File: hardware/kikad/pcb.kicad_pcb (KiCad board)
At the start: 2 copper layers, 55 x 55 mm, 22 parts, among them J1 Output

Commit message: implement binary build
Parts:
- D1, D2, D3, D4: footprint LED_THT:LED_D5.0mm-4_RGB_Wide_Pins -> LED_THT:LED_D5.0mm-4_RGB_Wide_Pins_CNC_read
- R1, R10, R11, R12, R13, R14, R2, R3, R4, R5, R6, R7, R8, R9: footprint Resistor_THT:R_Axial_DIN0204_L3.6mm_D1.6mm_P7.62mm_Horizontal -> Resistor_THT:CNC_Ready_R_Axial_DIN0204_L3.6mm_D1.6mm_P7.62mm_Horizontal
- U2: footprint esp_32_c3_supper_mini:PN532 NFC RFID -> esp_32_c3_supper_mini:PN532 NFC RFID simple (one row)
- moved BZ1 34.0 mm to (111.1, 60.2), turned to 180 degrees
- moved R13 18.4 mm to (122.5, 51.9), turned to 180 degrees
- moved R1 6.51 mm to (128.2, 42.8)
- moved R2 4.37 mm to (128.4, 45.5)
- moved R3 2.75 mm to (128.5, 48.4)
- moved D3 1.59 mm to (144.4, 92.1)
- moved D1 1.49 mm to (145.0, 43.6)
- moved D4 1.46 mm to (110.1, 92.0)
- moved R4 1.16 mm to (120.8, 48.3)
- moved R9 1.12 mm to (128.3, 93.0)
- moved R12 1.12 mm to (121.3, 93.0)
- moved D2 0.92 mm to (110.1, 43.4)
- moved R8 0.71 mm to (128.2, 90.3)
- moved R11 0.70 mm to (121.3, 90.3)
- moved R5 0.62 mm to (120.8, 45.5)
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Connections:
- R13 pad 1: Net-(U1-GPIO9/SCL) -> Net-(U1-GPIO21)
- U1 pad 13: Net-(U1-GPIO9/SCL) -> /R
- U1 pad 14: /R -> /G
- U1 pad 15: /G -> /B
- U1 pad 16: /B -> Net-(U1-GPIO21)
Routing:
- net Net-(U1-GPIO21): track 0.00 -> 20.1 mm
- net /R: track 105.5 -> 98.0 mm
- net Net-(U1-GPIO9/SCL): track 7.43 -> 0.00 mm
- net /G: track 91.3 -> 85.8 mm
- net /B: track 80.8 -> 75.5 mm
- net Net-(U1-GPIO8/SDA): track 21.9 -> 26.5 mm
- net Net-(D1-RA): track 4.93 -> 9.50 mm
- net Net-(U1-GPIO6/MOSI): track 24.0 -> 28.5 mm
- net Net-(U1-GPIO7/SS): track 20.4 -> 24.5 mm
- net Net-(U1-GPIO5/MISO): track 27.6 -> 31.1 mm
- net Net-(BZ1-+): track 6.59 -> 9.78 mm
- net Net-(D1-GA): track 12.5 -> 15.5 mm
- net Net-(D1-BA): track 17.4 -> 19.3 mm
- net Net-(D3-RA): track 10.3 -> 8.91 mm
- net Net-(D3-GA): track 16.3 -> 15.2 mm
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
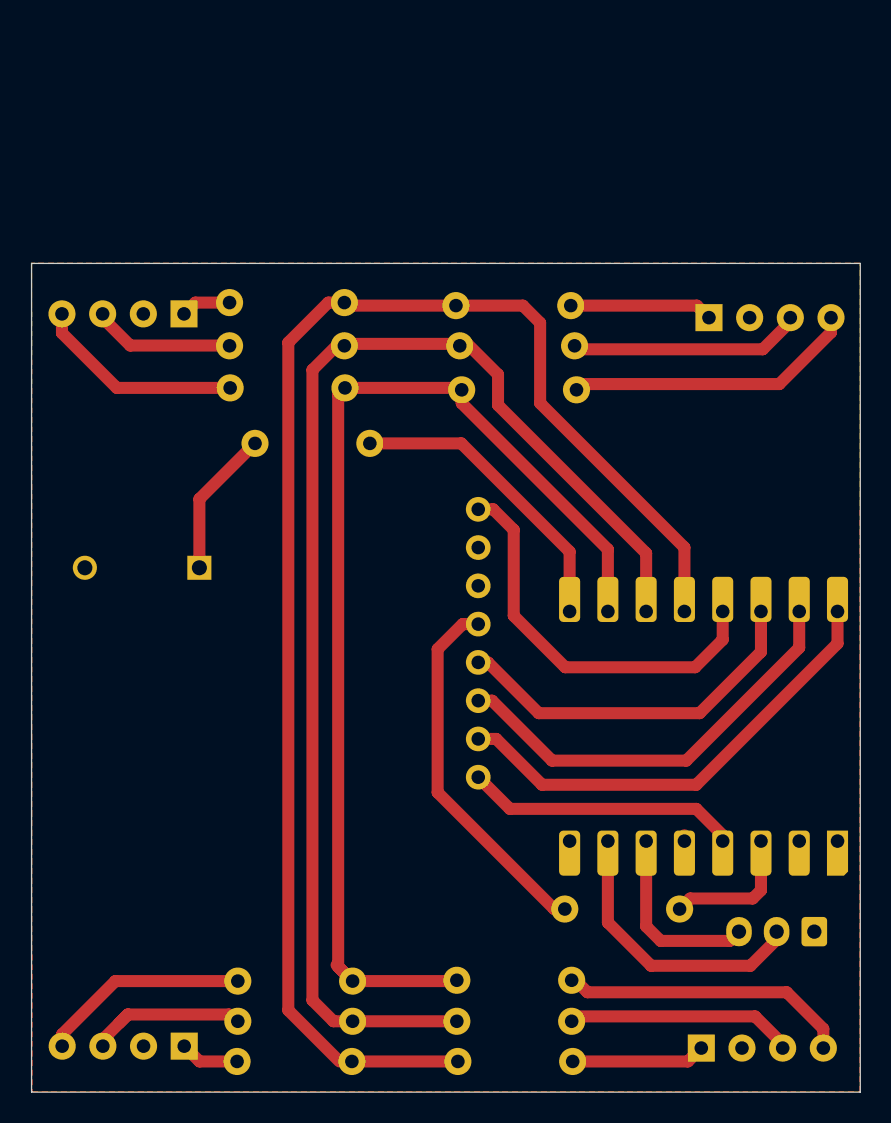
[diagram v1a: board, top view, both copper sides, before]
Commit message: update the kikad pcb, move buzzer to GPIO0
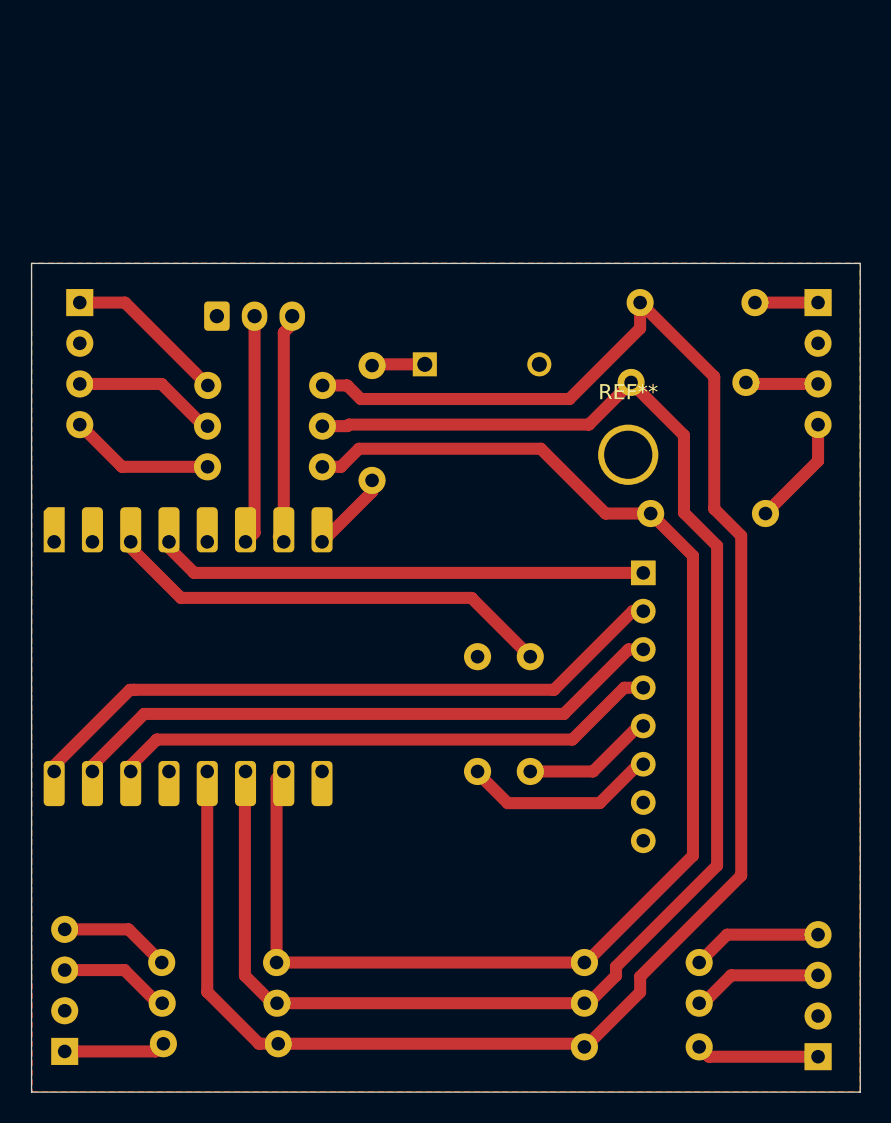
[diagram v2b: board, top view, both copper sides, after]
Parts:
- added R15: 0, Resistor_THT:CNC_Ready_R_Axial_DIN0204_L3.6mm_D1.6mm_P7.62mm_Horizontal, B.Cu at (129.6, 73.7)
- added REF**: MountingHole_3.2mm_M3, MountingHole:MountingHole_3.2mm_M3, F.Cu at (139.6, 52.7)
- moved J1 56.9 mm to (112.3, 43.5), turned to 0 degrees
- moved U1 32.3 mm to (111.5, 66.1), turned to -90 degrees
- moved BZ1 20.2 mm to (126.1, 46.7), turned to 0 degrees
- moved R3 15.0 mm to (141.1, 56.6)
- moved R1 12.2 mm to (140.4, 42.6)
- moved R2 11.6 mm to (139.8, 47.9)
- moved U2 9.91 mm to (127.1, 67.1), turned to -90 degrees
- moved R14 9.41 mm to (133.1, 73.7), turned to 90 degrees
- moved R8 8.55 mm to (136.7, 89.1)
- moved R7 8.55 mm to (136.7, 86.4)
- moved R9 8.45 mm to (136.7, 92.0)
- moved D4 7.94 mm to (102.2, 92.3), turned to 90 degrees
- moved D3 7.77 mm to (152.2, 92.7), turned to 90 degrees
- moved D1 7.31 mm to (152.2, 42.6), turned to -90 degrees
- moved D2 6.96 mm to (103.2, 42.6), turned to -90 degrees
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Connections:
- R13 pad 1: Net-(U1-GPIO21) -> Net-(U1-GPIO0)
- U1 pad 12: Net-(U1-GPIO8/SDA) -> unconnected-(U1-GPIO8/SDA-Pad12)
- U1 pad 16: Net-(U1-GPIO21) -> unconnected-(U1-GPIO21-Pad16)
- U1 pad 6: Net-(J1-Pin_3) -> Net-(J1-Pin_2)
- U1 pad 7: Net-(J1-Pin_2) -> Net-(J1-Pin_3)
- U1 pad 8: unconnected-(U1-GPIO0-Pad8) -> Net-(U1-GPIO0)
- U2 pad 10: GND -> Net-(R15-Pad1)
- U2 pad 12: Net-(U1-GPIO8/SDA) -> unconnected-(U2-RSTO-Pad12)
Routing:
- net Net-(U1-GPIO8/SDA): track 26.5 -> 0.00 mm
- net /R: track 98.0 -> 122.8 mm
- net Net-(U1-3V3): track 9.18 -> 29.9 mm
- net /G: track 85.8 -> 106.1 mm
- net Net-(U1-GPIO21): track 20.1 -> 0.00 mm
- net /B: track 75.5 -> 91.6 mm
- net Net-(R14-Pad1): track 24.9 -> 8.75 mm
- net Net-(U1-GPIO4/SCK): track 18.2 -> 32.6 mm
- net Net-(R15-Pad1): track 0.00 -> 12.9 mm
- net Net-(U1-GPIO5/MISO): track 31.1 -> 43.7 mm
- net Net-(U1-GPIO7/SS): track 24.5 -> 36.6 mm
- net Net-(D1-BA): track 19.3 -> 7.35 mm
- net Net-(U1-GPIO6/MOSI): track 28.5 -> 40.1 mm
- net Net-(D1-GA): track 15.5 -> 4.83 mm
- net Net-(D3-BA): track 19.3 -> 8.66 mm
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
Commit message: ad power for 5v esp
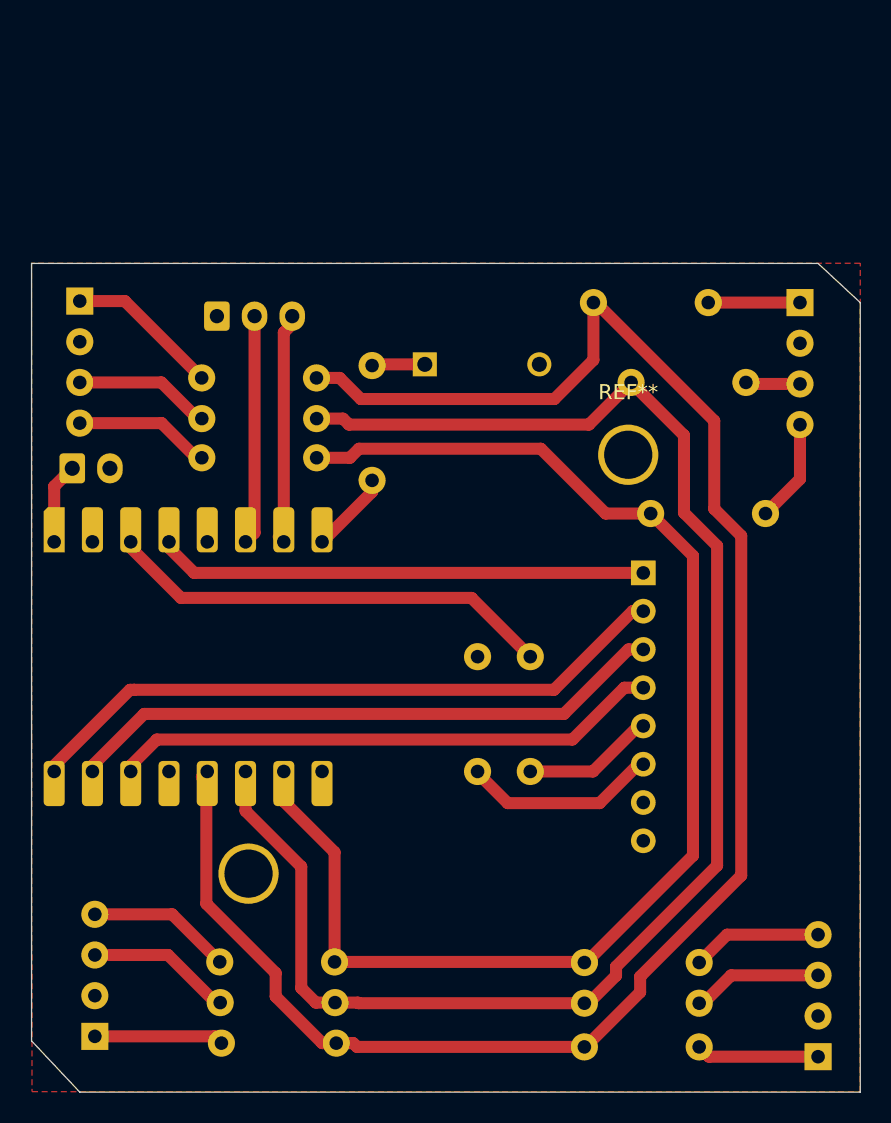
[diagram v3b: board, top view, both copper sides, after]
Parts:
- added ?: , , F.Cu at (114.4, 80.5)
- added J2: Conn_01x02_Pin, Connector_JST:JST_EH_B2B-EH-A_1x02_P2.50mm_Vertical, B.Cu at (102.7, 53.6)
- moved R10 3.85 mm to (120.1, 86.4)
- moved R11 3.85 mm to (120.1, 89.1)
- moved R12 3.85 mm to (120.2, 91.8)
- moved R1 3.10 mm to (137.3, 42.6)
- moved D4 2.24 mm to (104.2, 91.3)
- moved D1 1.20 mm to (151.0, 42.6)
- moved R4 0.71 mm to (118.9, 52.9)
- moved R6 0.65 mm to (118.9, 47.6)
- moved R5 0.63 mm to (118.9, 50.3)
- moved D2 0.10 mm to (103.2, 42.5)
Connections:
- U1 pad 1: unconnected-(U1-5V-Pad1) -> Net-(J2-Pin_1)
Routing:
- net Net-(J2-Pin_1): track 0.00 -> 5.38 mm
- net /B: track 91.6 -> 89.1 mm
- net Net-(D4-GA): track 7.38 -> 9.63 mm
- net Net-(D4-BA): track 7.35 -> 9.60 mm
- net Net-(D1-RA): track 4.19 -> 6.09 mm
- net Net-(D4-RA): track 6.76 -> 8.59 mm
- net /R: track 122.8 -> 121.3 mm
- net /G: track 106.1 -> 104.7 mm
- net Net-(D1-GA): track 4.83 -> 3.63 mm
- net Net-(D2-BA): track 9.78 -> 9.05 mm
- net Net-(D2-RA): track 10.8 -> 10.2 mm
- net Net-(D2-GA): track 9.64 -> 9.09 mm
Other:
- outline, holes or cut-outs redrawn

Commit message: use mac adress to create the prismo host and wifi
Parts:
- removed ?: , 
- removed J1: Output, Connector_JST:JST_XH_B3B-XH-A_1x03_P2.50mm_Vertical
- removed J2: Conn_01x02_Pin, Connector_JST:JST_EH_B2B-EH-A_1x02_P2.50mm_Vertical
- removed the REF** at (139.6, 52.7)
- added J3: Conn_01x04_Pin, TerminalBlock_Phoenix:TerminalBlock_Phoenix_MKDS-1,5-4-5.08_1x04_P5.08mm_Horizontal, F.Cu at (108.2, 31.9)
- added REF**: MountingHole_3.2mm_M3_DIN965, MountingHole:MountingHole_3.2mm_M3_DIN965, F.Cu at (114.4, 80.5)
- added REF**: MountingHole_3.2mm_M3_DIN965, MountingHole:MountingHole_3.2mm_M3_DIN965, F.Cu at (139.6, 52.7)
- D1, D2, D3, D4: footprint LED_THT:LED_D5.0mm-4_RGB_Wide_Pins_CNC_read -> LED_THT:LED_D5.0mm-4_RGB_Wide_Pins_CNC_read_angle
- moved D2 5.41 mm to (101.7, 47.7), turned to 90 degrees
- moved D3 5.40 mm to (146.8, 92.8)
- moved D4 4.27 mm to (108.2, 92.8), turned to 180 degrees
- moved D1 3.71 mm to (147.4, 41.7), turned to 0 degrees
- moved R9 1.52 mm to (135.3, 92.6)
- moved R12 0.88 mm to (120.2, 92.6)
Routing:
- net /R: track 121.3 -> 101.0 mm
- net Net-(J3-Pin_3): track 15.7 -> 0.42 mm
- net Net-(J3-Pin_4): track 15.7 -> 0.48 mm
- net Net-(D2-RA): track 10.2 -> 0.00 mm
- net Net-(D2-GA): track 9.09 -> 0.28 mm
- net Net-(D2-BA): track 9.05 -> 0.37 mm
- net Net-(D3-BA): track 8.66 -> 0.00 mm
- net Net-(D3-GA): track 8.66 -> 0.27 mm
- net Net-(D3-RA): track 8.16 -> 0.00 mm
- net Net-(D1-BA): track 6.85 -> 0.00 mm
- net Net-(D1-RA): track 6.09 -> 0.00 mm
- net Net-(J3-Pin_2): track 5.38 -> 0.00 mm
- net Net-(D4-RA): track 8.59 -> 4.46 mm
- net Net-(D1-GA): track 3.63 -> 0.14 mm
- net /B: track 89.1 -> 90.9 mm
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
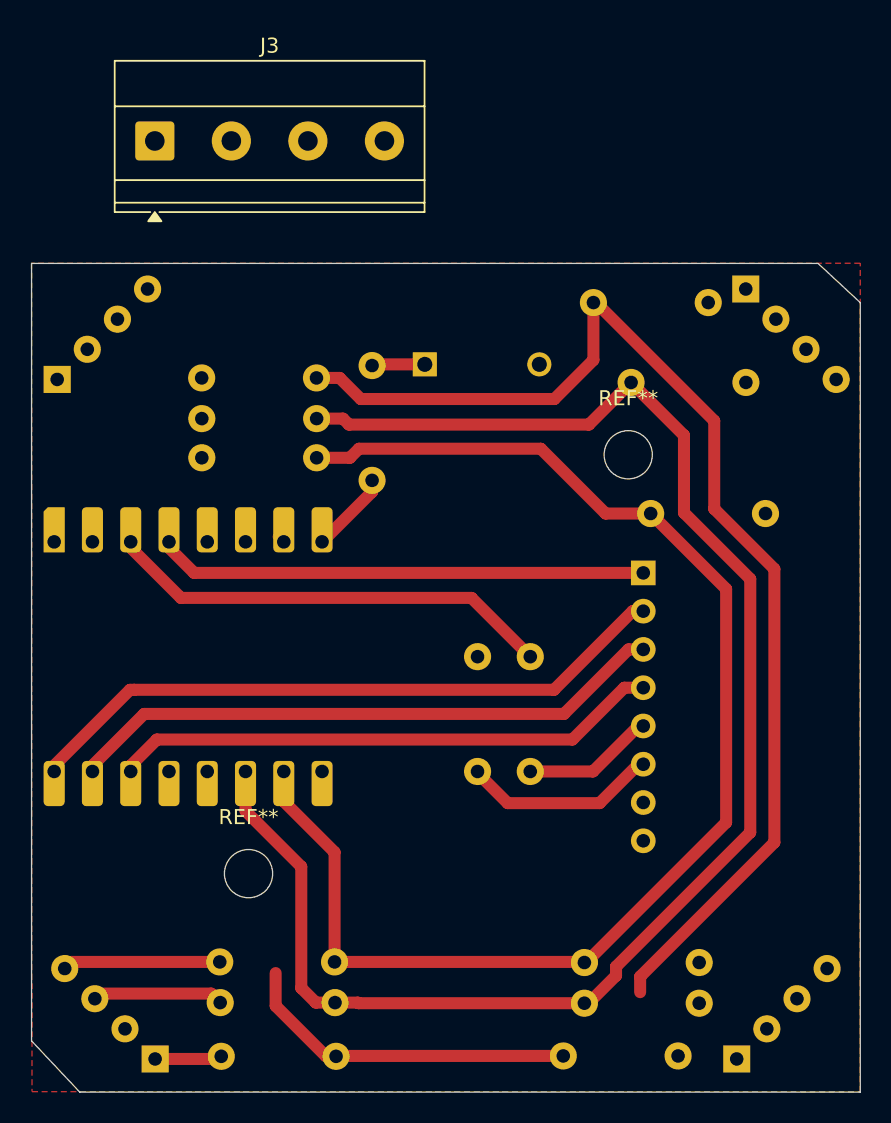
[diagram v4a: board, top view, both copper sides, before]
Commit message: new board, bottom layer, cut all corvers
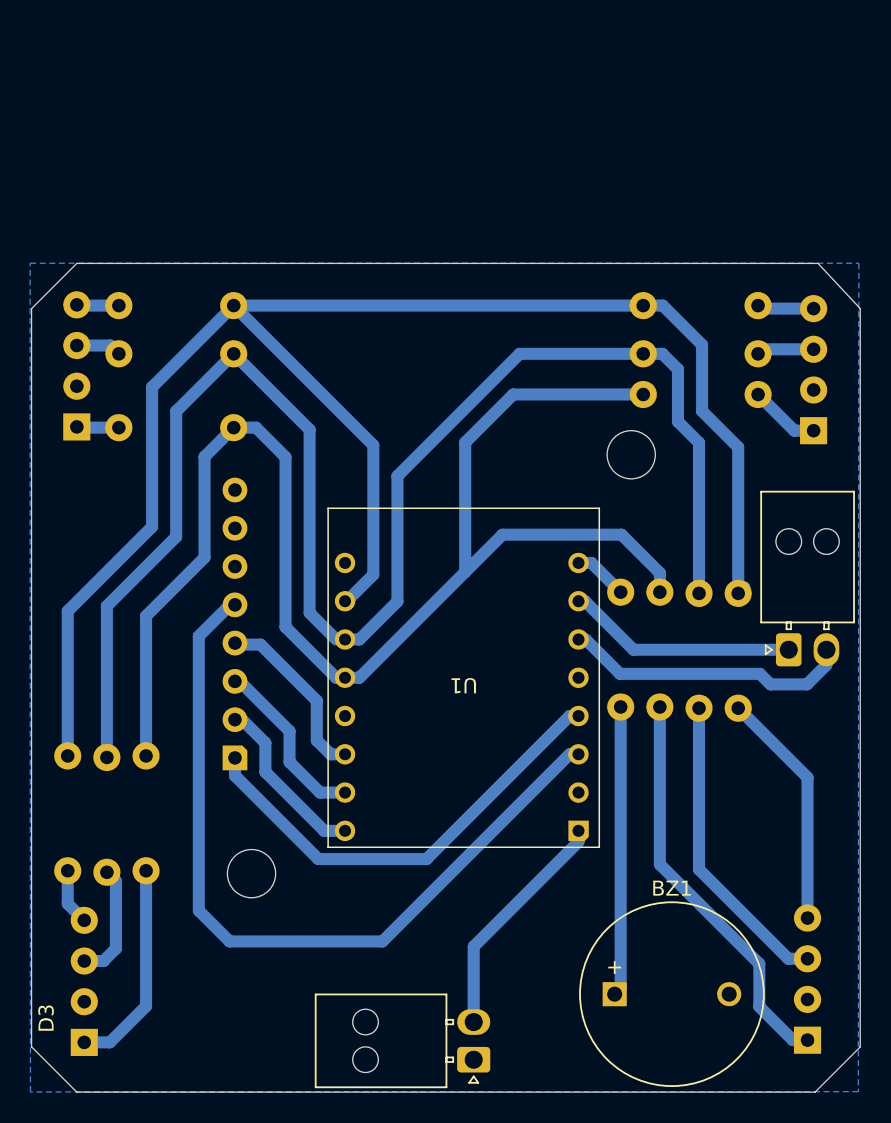
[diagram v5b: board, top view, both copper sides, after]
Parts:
- removed J3: Conn_01x04_Pin, TerminalBlock_Phoenix:TerminalBlock_Phoenix_MKDS-1,5-4-5.08_1x04_P5.08mm_Horizontal
- removed R14, R15: 0, Resistor_THT:CNC_Ready_R_Axial_DIN0204_L3.6mm_D1.6mm_P7.62mm_Horizontal
- added J1: Conn_01x02_Socket, Connector_Molex:Molex_Nano-Fit_105313-xx02_1x02_P2.50mm_Horizontal, F.Cu at (129.3, 92.8)
- added J2: Conn_01x02_Socket, Connector_Molex:Molex_Nano-Fit_105313-xx02_1x02_P2.50mm_Horizontal, F.Cu at (150.3, 65.6)
- BZ1, R1, R10, R11, R12, R13, R2, R3, R4, R5, R6, R7, R8, R9: moved to F.Cu
- D1, D2, D3, D4: footprint LED_THT:LED_D5.0mm-4_RGB_Wide_Pins_CNC_read_angle -> LED_THT:LED_D5.0mm-4_RGB_Wide_Pins_CNC_read; moved to F.Cu
- REF** (x2): moved to B.Cu
- U1: footprint esp_32_c3_supper_mini:esp_32_c3_supper_mini_tht_smd -> esp_32_c3_supper_mini:esp_32_c3_supper_mini; moved to F.Cu
- U2: footprint esp_32_c3_supper_mini:PN532 NFC RFID simple (one row) -> esp_32_c3_supper_mini:PN532 NFC RFID simple (one row) flip; moved to F.Cu
- moved D2 50.3 mm to (151.9, 51.1)
- moved D1 45.3 mm to (103.0, 50.9), turned to 90 degrees
- moved BZ1 43.7 mm to (138.7, 88.5)
- moved D4 43.3 mm to (151.5, 91.5), turned to 90 degrees
- moved D3 43.3 mm to (103.5, 91.7)
- moved R12 37.6 mm to (141.7, 61.8), turned to -90 degrees
- moved R7 36.9 mm to (102.4, 72.7), turned to -90 degrees
- moved R11 36.4 mm to (144.3, 61.9), turned to -90 degrees
- moved R10 36.3 mm to (146.9, 61.9), turned to -90 degrees
- moved R8 35.6 mm to (105.0, 72.8), turned to -90 degrees
- moved R9 34.1 mm to (107.6, 72.7), turned to -90 degrees
- moved R3 30.9 mm to (113.4, 42.8), turned to 180 degrees
- moved R2 26.4 mm to (113.4, 46.0), turned to 180 degrees
- moved R1 25.3 mm to (113.4, 50.9), turned to 180 degrees
- moved R4 23.9 mm to (140.6, 42.8), turned to 0 degrees
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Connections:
- U2 pad 10: Net-(R15-Pad1) -> GND
- U2 pad 9: Net-(R14-Pad1) -> Net-(U1-3V3)
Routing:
- net Net-(U1-GPIO5/MISO): track 43.7 -> 11.5 mm
- net Net-(U1-GPIO6/MOSI): track 40.1 -> 11.6 mm
- net Net-(U1-GPIO7/SS): track 36.6 -> 11.9 mm
- net Net-(U1-3V3): track 29.9 -> 52.7 mm
- net Net-(D4-RA): track 4.46 -> 26.7 mm
- net Net-(J2-Pin_2): track 0.42 -> 19.2 mm
- net /B: track 90.9 -> 108.9 mm
- net Net-(BZ1-+): track 3.53 -> 19.2 mm
- net Net-(J1-Pin_2): track 0.00 -> 15.6 mm
- net Net-(J2-Pin_1): track 0.48 -> 15.3 mm
- net Net-(D3-RA): track 0.00 -> 14.1 mm
- net Net-(R15-Pad1): track 12.9 -> 0.00 mm
- net Net-(D4-GA): track 9.15 -> 20.4 mm
- net Net-(R14-Pad1): track 8.75 -> 0.00 mm
- net Net-(D3-GA): track 0.27 -> 7.75 mm
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- added copper zone on B.Cu, net GND
- removed copper zone on F.Cu, net GND
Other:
- outline, holes or cut-outs redrawn
